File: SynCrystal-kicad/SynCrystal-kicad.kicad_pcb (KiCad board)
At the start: 2 copper layers, 89 x 111.8 mm, 94 parts, among them CN1 PJ-342, J1 ICSP, J4 Pause Button, J5 to DIN-6 Male, Q1 SS8050, Q2 SS8050, Q3 AO3400A, Q4 SS8050, SW1 Mode -, SW2 Mode +, SW3 Frame -, SW4 Frame +, SW5 Shaft_Pulse_Ratio, SW6 Guide/Follow, U1 74HCT14, U10 MCP4725, U2 ATmega328P-A, U3 AP2210N-3.3TRG1, U4 ECS-TXO-3225MV-160-TR, U5 LMC6482, U7 G3VM-61VY3(TR)

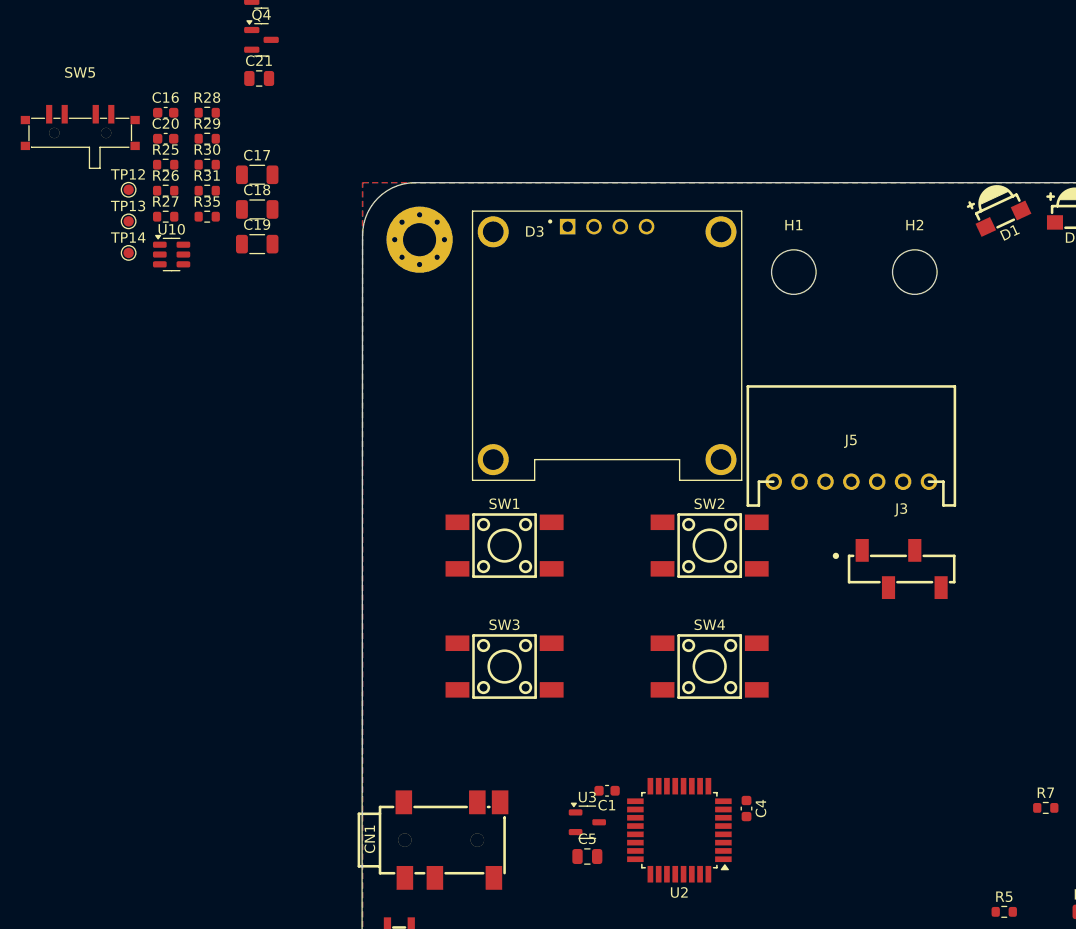
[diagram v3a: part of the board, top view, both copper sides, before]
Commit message: ERC now happy!
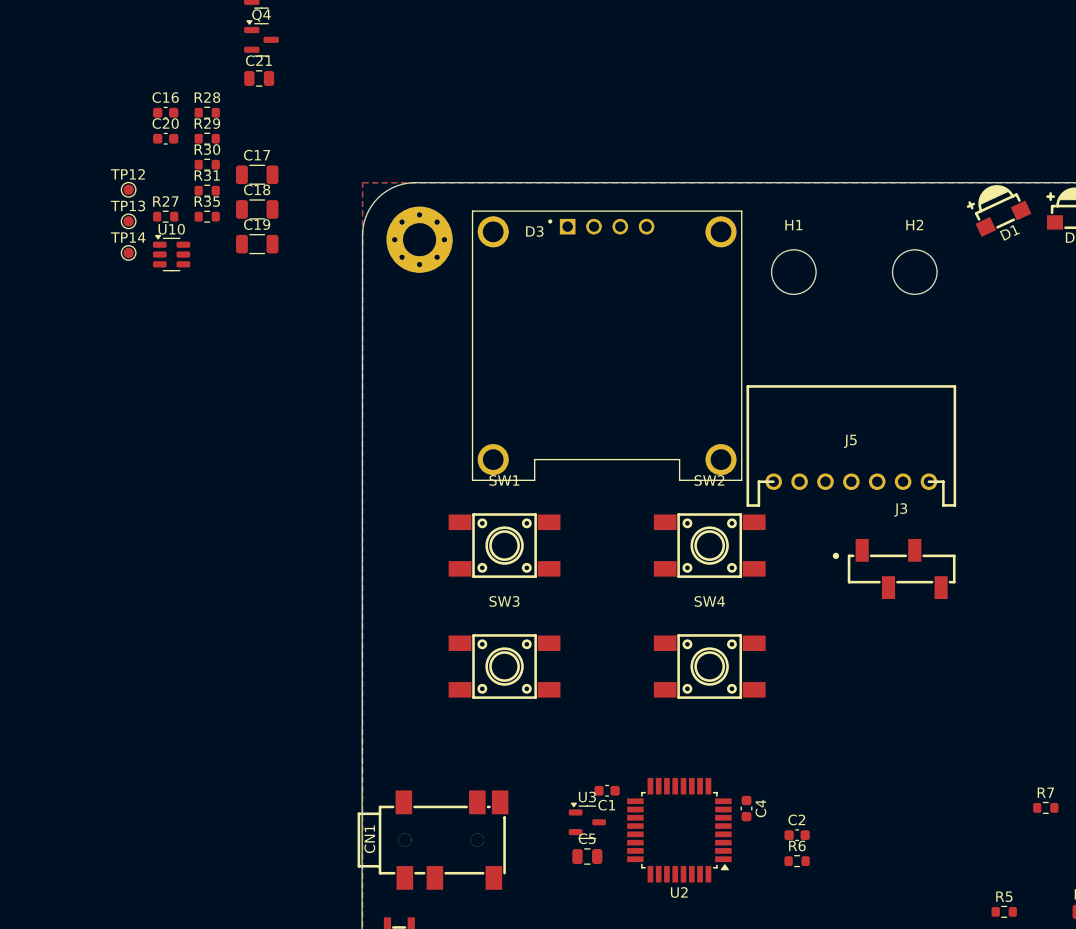
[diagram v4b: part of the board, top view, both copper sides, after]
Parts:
- removed R25, R26: 100k, Resistor_SMD:R_0603_1608Metric
- removed SW5: Shaft_Pulse_Ratio, easyEDA:SW-SMD_MSK13C02-SZ
- added C2: 100n, Capacitor_SMD:C_0603_1608Metric, F.Cu at (75.0, 83.3)
- added R6: 220k, Resistor_SMD:R_0603_1608Metric, F.Cu at (75.0, 85.9)
- SW1, SW2, SW3, SW4: footprint easyEDA:SW-SMD_4P-L6.0-W6.0-P4.50-LS9.0_TS-1002S-08026C -> easyEDA:KEY-SMD_4P-L6.0-W6.0-P4.50-LS8.6
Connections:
- J5 pad 5: GND -> /Proj_ID
- SW1 pad 1: unconnected-(SW1-Pad1) -> /Mode-
- SW1 pad 3: unconnected-(SW1-Pad3) -> GND
- SW2 pad 1: unconnected-(SW2-Pad1) -> /Mode+
- SW2 pad 3: unconnected-(SW2-Pad3) -> GND
- SW3 pad 1: unconnected-(SW3-Pad1) -> /Frame-
- SW3 pad 3: unconnected-(SW3-Pad3) -> GND
- SW4 pad 1: unconnected-(SW4-Pad1) -> /Frame+
- SW4 pad 3: unconnected-(SW4-Pad3) -> GND
- U2 pad 23: Net-(U2-PC0) -> /Proj_ID

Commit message: 90% routed
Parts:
- removed C20: 2u2, Capacitor_SMD:C_0603_1608Metric
- removed C21: 22u, Capacitor_SMD:C_0805_2012Metric
- removed J1: ICSP, Connector_PinHeader_2.54mm:PinHeader_2x03_P2.54mm_Vertical_displaced+
- removed R28: 470, Resistor_SMD:R_0603_1608Metric
- removed R29: 100k, Resistor_SMD:R_0603_1608Metric
- removed R30: 10k, Resistor_SMD:R_0603_1608Metric
- removed R31: 47, Resistor_SMD:R_0603_1608Metric
- removed R35: 220k, Resistor_SMD:R_0603_1608Metric
- removed REF**: MountingHole_3.2mm_M3_Pad_Via, MountingHole:MountingHole_3.2mm_M3_Pad_Via
- removed SW6: Guide/Follow, easyEDA:SW-TH_MSK12C02-HB-1
- removed TP14: Pause, TestPoint:TestPoint_Pad_D1.0mm
- removed TP3: D, TestPoint:TestPoint_Pad_D1.0mm
- removed TP4: Rx, TestPoint:TestPoint_Pad_D1.0mm
- removed U10: MCP4725, Package_TO_SOT_SMD:SOT-23-6
- added C10: 2u2, Capacitor_SMD:C_0603_1608Metric, F.Cu at (86.4, 57.1)
- added C3: 2u2, Capacitor_SMD:C_0603_1608Metric, F.Cu at (87.1, 88.8)
- added C7: 47u, Capacitor_SMD:C_1206_3216Metric, F.Cu at (51.8, 27.9)
- added D8: OLED 128x64, Peacemans Teile:OLED_128x63_i2c_0.96, F.Cu at (66.5, 57.9)
- added H3: MountingHole, MountingHole:MountingHole_3.2mm_M3_DIN965, F.Cu at (43.2, 25.4)
- added H4: MountingHole, MountingHole:MountingHole_3.2mm_M3_DIN965, F.Cu at (89.9, 25.4)
- added H5: MountingHole, MountingHole:MountingHole_3.2mm_M3_DIN965, F.Cu at (43.7, 109.5)
- added H6: MountingHole, MountingHole:MountingHole_3.2mm_M3_DIN965, F.Cu at (89.9, 109.5)
- added J2: to DIN-6 Male, easyEDA:CONN-TH_S7B-XH-A-LF-SN, F.Cu at (66.5, 41.8)
- added R10: 3k3, Resistor_SMD:R_0603_1608Metric, F.Cu at (90.4, 71.9)
- added R14: 10k, Resistor_SMD:R_0603_1608Metric, F.Cu at (84.3, 75.9)
- added R25: 2k2, Resistor_SMD:R_0603_1608Metric, F.Cu at (76.5, 110.9)
- added R26: 10k, Resistor_SMD:R_0603_1608Metric, F.Cu at (78.5, 110.9)
- added R9: 10k, Resistor_SMD:R_0603_1608Metric, F.Cu at (91.4, 58.1)
- added SW5: Frame +, easyEDA:KEY-SMD_4P-L6.0-W6.0-P4.50-LS8.6, F.Cu at (76.4, 88.1)
- added TP9: Imp IN, TestPoint:TestPoint_Pad_D1.0mm, F.Cu at (46.7, 41.7)
- added U6: LMC6482, Package_SO:SOIC-8_3.9x4.9mm_P1.27mm, F.Cu at (42.9, 77.5)
- C1, C8: value 100n -> 22u; footprint Capacitor_SMD:C_0603_1608Metric -> Capacitor_SMD:C_0805_2012Metric
- C15: value 330n -> 100n
- C16: value 100n -> 330n
- C17, C18: value 47u -> 100n; footprint Capacitor_SMD:C_1206_3216Metric -> Capacitor_SMD:C_0603_1608Metric
- C19: value 47u -> 1u; footprint Capacitor_SMD:C_1206_3216Metric -> Capacitor_SMD:C_0603_1608Metric
- C5: value 22u -> 47u; footprint Capacitor_SMD:C_0805_2012Metric -> Capacitor_SMD:C_1206_3216Metric
- C6: value 2u2 -> 47u; footprint Capacitor_SMD:C_0603_1608Metric -> Capacitor_SMD:C_1206_3216Metric
- D1, D5, D6: value LED -> B5819W SL; footprint easyEDA:LED-SMD_XYC-IRA4335A65-X4 -> Diode_SMD:D_SOD-123
- D2, D4: value B5819W SL -> LED; footprint Diode_SMD:D_SOD-123 -> easyEDA:LED-SMD_XYC-IRA4335A65-X4
- D3: value OLED 128x64 -> LED; footprint Peacemans Teile:OLED_128x63_i2c_0.96 -> easyEDA:LED-SMD_XYC-IRA4335A65-X4
- H1, H2: footprint MountingHole:MountingHole_4.3mm_M4_ISO14580 -> MountingHole:MountingHole_3.2mm_M3_DIN965
- J3: value ~ -> Pause Button; footprint easyEDA:HDR-SMD_HX-PM2.54-1X4P-TP-YQ -> easyEDA:CONN-TH_2P-P2.54_MX128-2.54-GN01-02P-CU-Y-A
- J4: value Pause Button -> ICSP; footprint easyEDA:CONN-TH_2P-P2.54_MX128-2.54-GN01-02P-CU-Y-A -> Peacemans Teile:PinHeader_2x03_P2.54mm_Vertical_displaced
- J5: value to DIN-6 Male -> ~; footprint easyEDA:CONN-TH_S7B-XH-A-LF-SN -> easyEDA:HDR-SMD_HX-PM2.54-1X4P-TP-YQ
- Q1: value SS8050 -> AO3400A
- Q3: value AO3400A -> SS8050
- R1: value 2k2 -> 47
- R11: value 3k3 -> 47k
- R12: value 100k -> 470k
- R13: value 10k -> 3k3
- R15, R16: value 10k -> 220k
- R17: value 5R1 -> 10k; footprint Resistor_SMD:R_0805_2012Metric -> Resistor_SMD:R_0603_1608Metric
- R18: value 100k -> 10k
- R2: value 2k2 -> 5R1; footprint Resistor_SMD:R_0603_1608Metric -> Resistor_SMD:R_0805_2012Metric
- R21: value 47 -> 100k
- R22: value 10 -> 47
- R23: value 22k -> 220k
- R24: value 100 -> 2k2
- R27: value 10k -> 100k
- R3: value 10k -> 10
- R4: value 220k -> 22k
- R5: value 3k3 -> 100
- R6: value 220k -> 10k
- R7: value 47k -> 470
- R8: value 470k -> 100k
- SW1: value Mode - -> Guide/Follow; footprint easyEDA:KEY-SMD_4P-L6.0-W6.0-P4.50-LS8.6 -> easyEDA:SW-TH_MSK12C02-HB-1
- SW2: value Mode + -> Mode -
- SW3: value Frame - -> Mode +
- SW4: value Frame + -> Frame -
- TP1: value P -> 3V3
- TP10: value Imp IN -> Imp cln
- TP11: value Imp cln -> D
- TP12: value DAC -> Rx
- TP13: value Pause -> Tx
- TP2: value I -> 5V
- TP5: value Tx -> DAC
- TP6: value fps pulse -> P
- TP7: value 5V -> I
- TP8: value 3V3 -> fps pulse
- U1: value 74HCT14 -> ECS-TXO-3225MV-160-TR; footprint Package_SO:TSSOP-14_4.4x5mm_P0.65mm -> Crystal:Crystal_SMD_3225-4Pin_3.2x2.5mm
- U2: value ATmega328P-A -> AP2210N-3.3TRG1; footprint Package_QFP:TQFP-32_7x7mm_P0.8mm -> Package_TO_SOT_SMD:SOT-23-3
- U3: value AP2210N-3.3TRG1 -> 74HCT14; footprint Package_TO_SOT_SMD:SOT-23-3 -> Package_SO:TSSOP-14_4.4x5mm_P0.65mm
- U4: value ECS-TXO-3225MV-160-TR -> G3VM-61VY3(TR); footprint Crystal:Crystal_SMD_3225-4Pin_3.2x2.5mm -> easyEDA:SOP-4_L3.9-W4.4-P2.54-LS7.0-BR
- U5: value LMC6482 -> MCP4725; footprint Package_SO:SOIC-8_3.9x4.9mm_P1.27mm -> Package_TO_SOT_SMD:SOT-23-6
- U7: value G3VM-61VY3(TR) -> ATmega328P-A; footprint easyEDA:SOP-4_L3.9-W4.4-P2.54-LS7.0-BR -> Package_QFP:TQFP-32_7x7mm_P0.8mm
- moved Q4 118.9 mm to (92.1, 103.5), turned to 90 degrees
- moved C6 117.3 mm to (51.8, 31.0), turned to 0 degrees
- moved R15 116.7 mm to (48.0, 32.3)
- moved R16 115.6 mm to (48.0, 35.8)
- moved TP12 114.8 mm to (82.0, 110.7), turned to 90 degrees
- moved R20 114.5 mm to (47.8, 77.2), turned to 0 degrees
- moved R2 114.5 mm to (51.9, 39.6), turned to 0 degrees
- moved R19 114.3 mm to (47.8, 74.2), turned to 0 degrees
- moved TP13 114.1 mm to (84.6, 110.7), turned to 90 degrees
- moved R18 114.1 mm to (47.8, 80.3), turned to 180 degrees
- moved C14 100.9 mm to (50.8, 75.4), turned to -90 degrees
- moved C11 100.0 mm to (72.2, 55.3), turned to 180 degrees
- moved C19 98.6 mm to (84.1, 103.6), turned to 90 degrees
- moved C17 98.2 mm to (68.3, 106.6), turned to 90 degrees
- moved Q3 98.0 mm to (87.5, 75.9)
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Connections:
- C1 pad 1: Net-(U2-AREF) -> Net-(CGQ1-VCC)
- C12 pad 1: GND -> Net-(C12-Pad1)
- C12 pad 2: +5V -> GND
- C13 pad 1: Net-(D2-A) -> Net-(U7-AREF)
- C13 pad 2: Net-(U5B-+) -> GND
- C14 pad 1: Net-(Q2-B) -> Net-(D6-A)
- C14 pad 2: /INT1 -> Net-(U6B-+)
- C15 pad 1: GND -> Net-(Q4-B)
- C15 pad 2: Net-(C15-Pad2) -> /INT1
- C16 pad 1: +5V -> GND
- C16 pad 2: GND -> Net-(C16-Pad2)
- C17 pad 1: +5V -> /Proj_ID
- C18 pad 1: +5V -> GND
- C18 pad 2: GND -> +5V
- C19 pad 1: +5V -> GND
- C19 pad 2: GND -> +5V
- C2 pad 1: /Proj_ID -> +3.3V
- C4 pad 1: +3.3V -> +5V
- C6 pad 1: +3.3V -> +5V
- C8 pad 1: Net-(C8-Pad1) -> +5V
- CGQ1 pad 1: /D_POT -> Net-(CGQ1-VOUT)
- D1 pad 1: Net-(D1-K) -> /D_POT
- D1 pad 2: Net-(D1-A) -> Net-(CGQ1-VOUT)
- D2 pad 1: +5V -> Net-(D2-K)
- D3 pad 1: Net-(D3-GND) -> Net-(D2-A)
- D3 pad 2: Net-(D3-VCC) -> Net-(D3-A)
- D4 pad 1: Net-(D2-A) -> Net-(D3-A)
- D4 pad 2: GND -> Net-(D4-A)
- D5 pad 2: Net-(D1-K) -> Net-(D5-A)
- D6 pad 1: Net-(D6-K) -> +5V
- D6 pad 2: Net-(D5-K) -> Net-(D6-A)
- D7 pad 1: Net-(D7-K) -> Net-(D6-A)
- D7 pad 2: Net-(D7-A) -> GND
- J3 pad 1: /In_Sync-LED -> Net-(J3-Pin_1)
- J3 pad 2: /DAC_EN -> Net-(J3-Pin_2)
- J4 pad 1: Net-(J4-Pin_1) -> /MISO
- J4 pad 2: Net-(J4-Pin_2) -> +5V
- J5 pad 1: /Stop_EN -> /In_Sync-LED
- J5 pad 2: /M-Pin -> /DAC_EN
- J5 pad 3: +5V -> /Ext_Imp_LED
- J5 pad 4: /Ctrl_V -> GND
- JP1 pad 1: Net-(D3-VCC) -> Net-(D8-VCC)
- JP2 pad 1: Net-(D3-GND) -> Net-(D8-GND)
- JP2 pad 3: Net-(D3-VCC) -> Net-(D8-VCC)
- Q1 pad 1: Net-(Q1-B) -> Net-(Q1-G)
- Q1 pad 3: Net-(Q1-C) -> Net-(D2-K)
- Q2 pad 2: GND -> Net-(Q2-E)
- Q2 pad 3: /Ext_Imp_LED -> +5V
- Q3 pad 1: Net-(Q3-G) -> Net-(Q3-B)
- Q3 pad 3: Net-(D6-K) -> Net-(Q3-C)
- Q4 pad 2: Net-(Q4-E) -> GND
- Q4 pad 3: +5V -> /Ext_Imp_LED
- R1 pad 1: /SDA -> +5V
- R1 pad 2: +5V -> Net-(CGQ1-VCC)
- R11 pad 1: Net-(R11-Pad1) -> +5V
- R11 pad 2: Net-(C8-Pad1) -> Net-(Q3-B)
- R12 pad 1: +5V -> Net-(Q3-B)
- R12 pad 2: /Stop_EN -> Net-(Q3-C)
- R13 pad 1: Net-(D2-A) -> Net-(R13-Pad1)
- R13 pad 2: Net-(CN1-Pad5) -> Net-(C12-Pad1)
- R15 pad 1: /M-Pin -> +5V
- R15 pad 2: Net-(Q1-B) -> Net-(SW1-A)
- R16 pad 1: Net-(C15-Pad2) -> GND
- R16 pad 2: Net-(R16-Pad2) -> Net-(SW1-C)
- R17 pad 1: +5V -> Net-(D6-A)
- R17 pad 2: Net-(D1-A) -> Net-(CN1-Pad5)
- R18 pad 1: GND -> Net-(C16-Pad2)
- R18 pad 2: Net-(D2-A) -> Net-(R18-Pad2)
- R19 pad 2: Net-(U5B-+) -> Net-(D6-A)
- R2 pad 2: /SCL -> Net-(D4-A)
- R20 pad 1: Net-(Q2-B) -> GND
- R20 pad 2: GND -> Net-(U6B-+)
- R21 pad 1: Net-(R21-Pad1) -> Net-(Q4-B)
- R22 pad 1: /IRSEND -> Net-(R22-Pad1)
- R22 pad 2: Net-(Q3-G) -> GND
- R23 pad 1: /IRSEND -> /Proj_ID
- R24 pad 1: Net-(D7-A) -> /SDA
- R24 pad 2: /IRSEND -> +5V
- R27 pad 1: Net-(D7-K) -> +5V
- R27 pad 2: Net-(Q4-B) -> /Stop_EN
- R3 pad 1: +5V -> /IRSEND
- R3 pad 2: /~{RST} -> Net-(Q1-G)
- R4 pad 1: +5V -> /IRSEND
- R4 pad 2: Net-(SW6-A) -> GND
- R5 pad 1: Net-(Q1-C) -> Net-(D5-A)
- R5 pad 2: +5V -> /IRSEND
- R6 pad 1: /Proj_ID -> Net-(D5-K)
- R6 pad 2: GND -> Net-(Q2-B)
- R7 pad 1: +5V -> Net-(Q2-E)
- R7 pad 2: Net-(Q1-B) -> Net-(R7-Pad2)
- R8 pad 1: Net-(Q1-B) -> Net-(D5-K)
- R8 pad 2: Net-(Q1-C) -> GND
- RV1 pad 1: Net-(R21-Pad1) -> Net-(R22-Pad1)
- RV1 pad 2: Net-(U5B--) -> Net-(U6B--)
- RV1 pad 3: Net-(R16-Pad2) -> Net-(R18-Pad2)
- SW1 pad 1: /Mode- -> Net-(SW1-A)
- SW1 pad 2: /Mode- -> /MISO
- SW1 pad 3: GND -> Net-(SW1-C)
- SW2 pad 1: /Mode+ -> /Mode-
- SW2 pad 2: /Mode+ -> /Mode-
- SW3 pad 1: /Frame- -> /Mode+
- SW3 pad 2: /Frame- -> /Mode+
- SW4 pad 1: /Frame+ -> /Frame-
- SW4 pad 2: /Frame+ -> /Frame-
- TP1 pad 1: /P_POT -> +3.3V
- TP10 pad 1: Net-(CN1-Pad5) -> /INT1
- TP11 pad 1: /INT1 -> /D_POT
- TP12 pad 1: /Ctrl_V -> /RX
- TP13 pad 1: Net-(J4-Pin_2) -> /TX
- TP2 pad 1: /I_POT -> +5V
- TP5 pad 1: /TX -> /Ctrl_V
- TP6 pad 1: /MOSI -> /P_POT
- TP7 pad 1: +5V -> /I_POT
- TP8 pad 1: +3.3V -> /MOSI
- U1 pad 1: Net-(C15-Pad2) -> unconnected-(U1-Tri-State-Pad1)
- U1 pad 2: Net-(U1-Pad2) -> GND
- U1 pad 3: Net-(U4-Output) -> Net-(U1-Output)
- U1 pad 4: Net-(U1-Pad4) -> +3.3V
- U2 pad 1: /INT1 -> GND
- U2 pad 2: /Frame- -> +3.3V
- U2 pad 3: GND -> +5V
- U3 pad 1: GND -> Net-(C16-Pad2)
- U3 pad 2: +3.3V -> Net-(U3-Pad2)
- U3 pad 3: +5V -> Net-(U1-Output)
- U4 pad 1: unconnected-(U4-Tri-State-Pad1) -> Net-(R7-Pad2)
- U4 pad 3: Net-(U4-Output) -> Net-(J3-Pin_1)
- U4 pad 4: +3.3V -> Net-(J3-Pin_2)
- U5 pad 1: Net-(U5A--) -> /Ctrl_V
- U5 pad 2: Net-(U5A--) -> GND
- U5 pad 3: GND -> +5V
- U5 pad 4: GND -> /SDA
- U5 pad 5: Net-(U5B-+) -> /SCL
- U5 pad 6: Net-(U5B--) -> GND
- U7 pad 1: Net-(R28-Pad2) -> /INT1
- U7 pad 2: GND -> /Frame-
- U7 pad 3: Net-(J4-Pin_2) -> GND
- U7 pad 4: Net-(J4-Pin_1) -> +5V
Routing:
- net /MISO: track 0.00 -> 94.1 mm, vias 0 -> 2
- net /D_POT: track 0.00 -> 92.4 mm, vias 0 -> 6
- net /DAC_EN: track 0.00 -> 81.8 mm, vias 0 -> 2
- net /SCL: track 0.00 -> 74.7 mm, vias 0 -> 3
- net /Proj_ID: track 0.00 -> 73.4 mm, vias 0 -> 2
- net /IRSEND: track 0.00 -> 73.1 mm, vias 0 -> 2
- net /SDA: track 0.00 -> 67.2 mm, vias 0 -> 3
- net +5V: track 1.58 -> 61.2 mm, vias 0 -> 19
- net /Stop_EN: track 0.00 -> 59.3 mm, vias 0 -> 2
- net /Frame-: track 0.00 -> 58.6 mm, vias 0 -> 4
- net Net-(C16-Pad2): track 0.00 -> 57.4 mm, vias 0 -> 4
- net /Ext_Imp_LED: track 0.00 -> 47.9 mm, vias 0 -> 4
- net /M-Pin: track 0.00 -> 45.5 mm, vias 0 -> 1
- net /Mode+: track 0.00 -> 43.0 mm, vias 0 -> 2
- net /Mode-: track 0.00 -> 37.8 mm, vias 0 -> 2
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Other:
- board size 89 x 111.8 mm -> 56.4 x 94.2 mm
- board text added: "Follow-Switch Größer & THT 3.5mm THT Poti THT TPs THT"
- board text removed: "UI Anordnen ESS an Bus?"

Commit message: Looking good! Stil gotta run DRC
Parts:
- removed CN1: PJ-342, easyEDA:AUDIO-SMD_PJ-342
- removed H2: MountingHole, MountingHole:MountingHole_3.2mm_M3_DIN965
- added CN2: PJ-307N5, easyEDA:AUDIO-TH_PJ-307N5, F.Cu at (46.0, 39.4)
- H1: footprint MountingHole:MountingHole_3.2mm_M3_DIN965 -> Peacemans Teile:Kabelbinder 3mm
- SW1: footprint easyEDA:SW-TH_MSK12C02-HB-1 -> easyEDA:SW-TH_SS-12D11G4R
- TP1, TP10, TP11, TP12, TP13, TP2, TP5, TP6, TP7, TP8, TP9: footprint TestPoint:TestPoint_Pad_D1.0mm -> TestPoint:TestPoint_THTPad_1.5x1.5mm_Drill0.7mm
- moved R15 68.3 mm to (57.0, 100.0), turned to 180 degrees
- moved SW1 63.6 mm to (49.1, 97.9), turned to 90 degrees
- moved R16 60.3 mm to (56.9, 95.5), turned to 180 degrees
- moved TP8 32.2 mm to (59.5, 109.6)
- moved TP5 31.3 mm to (90.4, 82.3)
- moved TP10 26.1 mm to (62.3, 109.6)
- moved TP11 13.6 mm to (54.8, 109.5)
- moved TP7 13.6 mm to (52.0, 109.5)
- moved TP6 13.6 mm to (49.2, 109.5)
- moved R2 13.2 mm to (42.3, 30.5)
- moved C4 10.6 mm to (52.7, 26.0)
- moved TP9 7.00 mm to (44.3, 48.2), turned to -90 degrees
- moved C5 5.82 mm to (48.3, 29.4), turned to -90 degrees
- moved H1 5.52 mm to (66.5, 25.3)
- moved TP2 4.08 mm to (90.5, 85.6)
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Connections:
- R18 pad 1: Net-(C16-Pad2) -> Net-(R18-Pad1)
- R18 pad 2: Net-(R18-Pad2) -> Net-(C16-Pad2)
- RV1 pad 3: Net-(R18-Pad2) -> Net-(R18-Pad1)
- U6 pad 7: Net-(R18-Pad2) -> Net-(R18-Pad1)
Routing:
- net /Ctrl_V: track 22.1 -> 58.2 mm, vias 2 -> 3
- net /INT1: track 4.32 -> 39.4 mm, vias 0 -> 2
- net Net-(R18-Pad1): track 0.00 -> 32.5 mm
- net Net-(R18-Pad2): track 32.1 -> 0.00 mm
- net /MOSI: track 0.00 -> 27.1 mm
- net /D_POT: track 92.4 -> 107.6 mm, vias 6 -> 4
- net Net-(D4-A): track 23.4 -> 8.15 mm
- net /Mode-: track 37.8 -> 48.3 mm, vias 2 -> 4
- net /P_POT: track 20.1 -> 26.8 mm, vias 2 -> 0
- net +5V: track 61.2 -> 67.2 mm, vias 19 -> 21
- net /I_POT: track 18.9 -> 24.1 mm, vias 2 -> 0
- net Net-(R15-Pad2): track 0.00 -> 3.80 mm
- net Net-(R16-Pad2): track 0.00 -> 3.43 mm
- net Net-(Q3-C): track 30.3 -> 31.7 mm
- net /MISO: track 94.1 -> 93.1 mm, vias 2 -> 3
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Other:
- board text added: "3V3"
- board text added: "5V"
- board text added: "D"
- board text added: "DAC"
- board text added: "ESS"
- board text added: "Follow"
- board text added: "Guide"
- board text added: "I"
- board text added: "ICSP"
- board text added: "Imp. in"
- board text added: "P"
- board text added: "Rx"
- board text added: "Tx"
- board text added: "X"
- board text removed: "Follow-Switch Größer & THT 3.5mm THT Poti THT TPs THT"

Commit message: DRC happy, me happy.
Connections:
- CN2 pad 2: GND -> Net-(CN2-Pad2)
- CN2 pad 4: Net-(CN2-Pad4) -> GND
- R17 pad 2: Net-(CN2-Pad4) -> Net-(CN2-Pad2)
- TP9 pad 1: Net-(CN2-Pad4) -> Net-(CN2-Pad2)
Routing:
- net /MISO: track 93.1 -> 25.7 mm, vias 3 -> 2
- net Net-(CN2-Pad4): track 33.2 -> 0.00 mm, vias 2 -> 0
- net Net-(CN2-Pad2): track 0.00 -> 30.7 mm, vias 0 -> 2
- net Net-(C12-Pad1): track 2.49 -> 6.50 mm
- net Net-(CGQ1-VOUT): track 4.87 -> 7.38 mm
- net Net-(U6B--): track 19.8 -> 21.6 mm
- net /I_POT: track 24.1 -> 24.8 mm
- net /~{RST}: track 21.0 -> 21.5 mm
- net +5V: track 67.2 -> 67.7 mm, vias 21 -> 22

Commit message: Rev.A, orderable
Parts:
- J5: value ~ -> LED-Connector; footprint easyEDA:HDR-SMD_HX-PM2.54-1X4P-TP-YQ -> easyEDA:HDR-TH_6P-P2.00-V-F-R2-C3-S2.00-2
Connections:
- J5 pad 2: /DAC_EN -> GND
- J5 pad 3: /Ext_Imp_LED -> /DAC_EN
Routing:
- net /Mode-: track 48.3 -> 49.3 mm
- net /DAC_EN: track 81.8 -> 82.5 mm
- net /Ext_Imp_LED: track 48.4 -> 47.8 mm, vias 4 -> 3
- net /In_Sync-LED: vias 2 -> 3
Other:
- board text added: "Crystal Clock & ESS Precision for Vintage Projectors"
- board text added: "Impulswerk Controller"
- board text added: "JLCJLCJLCJLC"
- board text added: "Rev.A by filmkorn.org"
